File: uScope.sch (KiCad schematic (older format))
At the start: 20 parts

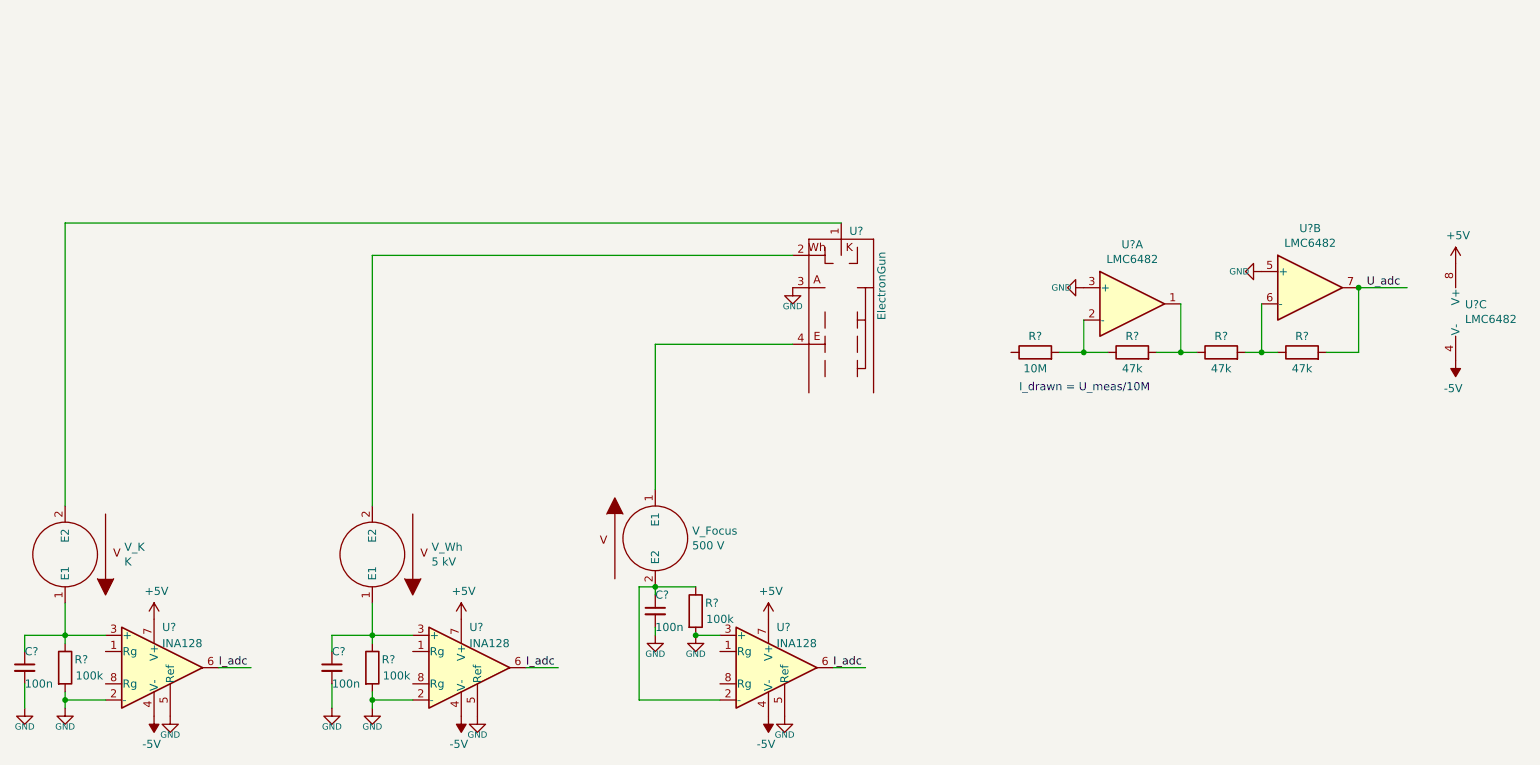
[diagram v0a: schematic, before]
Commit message: - schematic as hierarchical - added cache lib
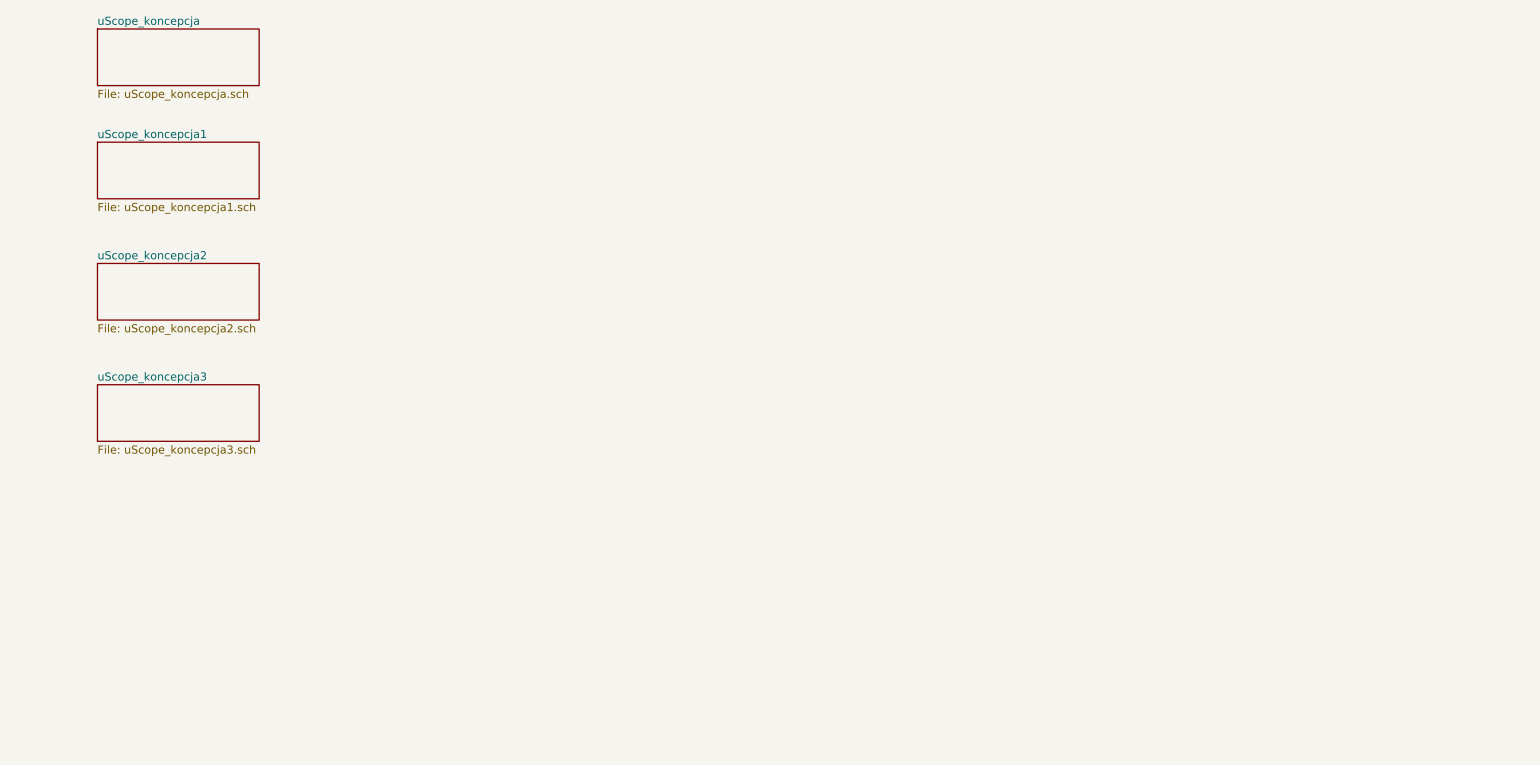
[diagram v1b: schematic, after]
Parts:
- removed C? (x3): 100n, symbol Device:C_Small
- removed R? (x3): 47k, symbol Device:R
- removed R?: 10M, symbol Device:R
- removed R? (x3): 100k, symbol Device:R
- removed U?: ElectronGun, symbol uScope:ElectronGun
- removed U? (x3): LMC6482, symbol Amplifier_Operational:LMC6482
- removed U? (x3): INA128, symbol Amplifier_Instrumentation:INA128
- removed V_Focus: 500 V, symbol pspice:VSOURCE
- removed V_K: K, symbol pspice:VSOURCE
- removed V_Wh: 5 kV, symbol pspice:VSOURCE
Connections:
- net labels removed: +5V, -5V, GND, I_adc, U_adc
- wire segments 46 -> 0
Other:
- note removed: "I_drawn = U_meas/10M"

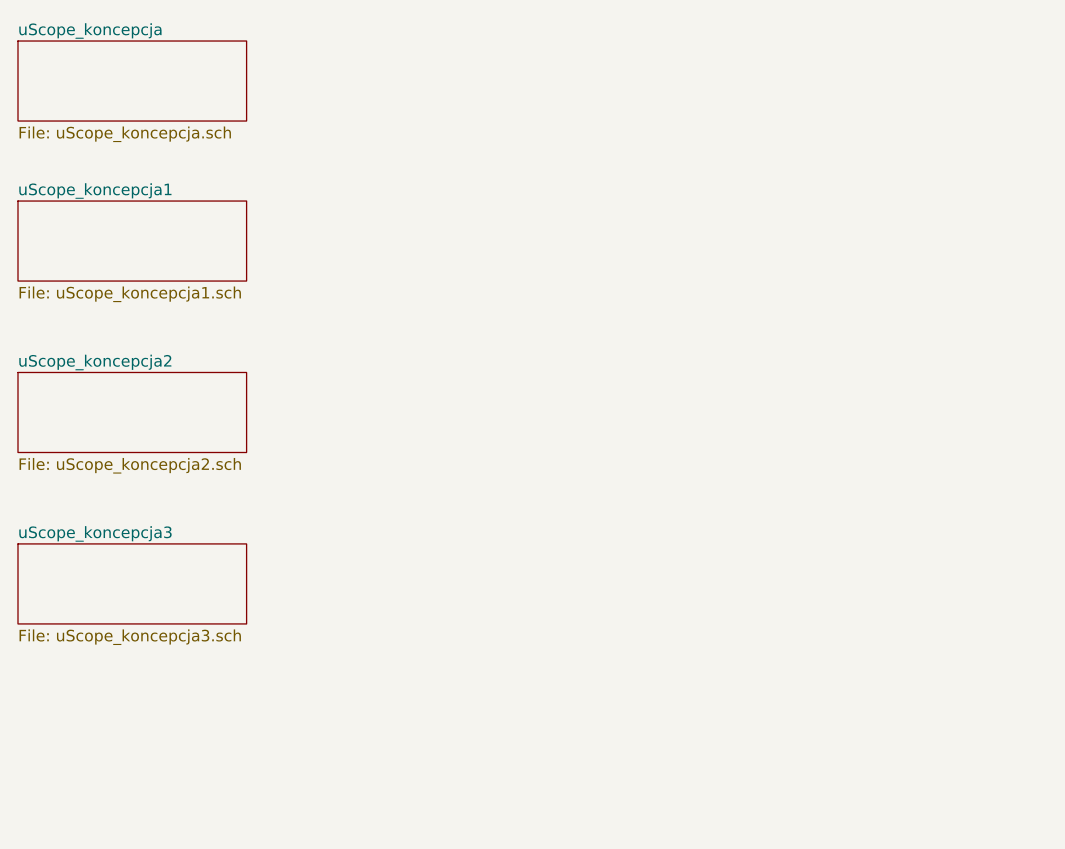
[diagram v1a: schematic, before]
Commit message: - moved voltmeters to separate sheet - hierarchical sheets
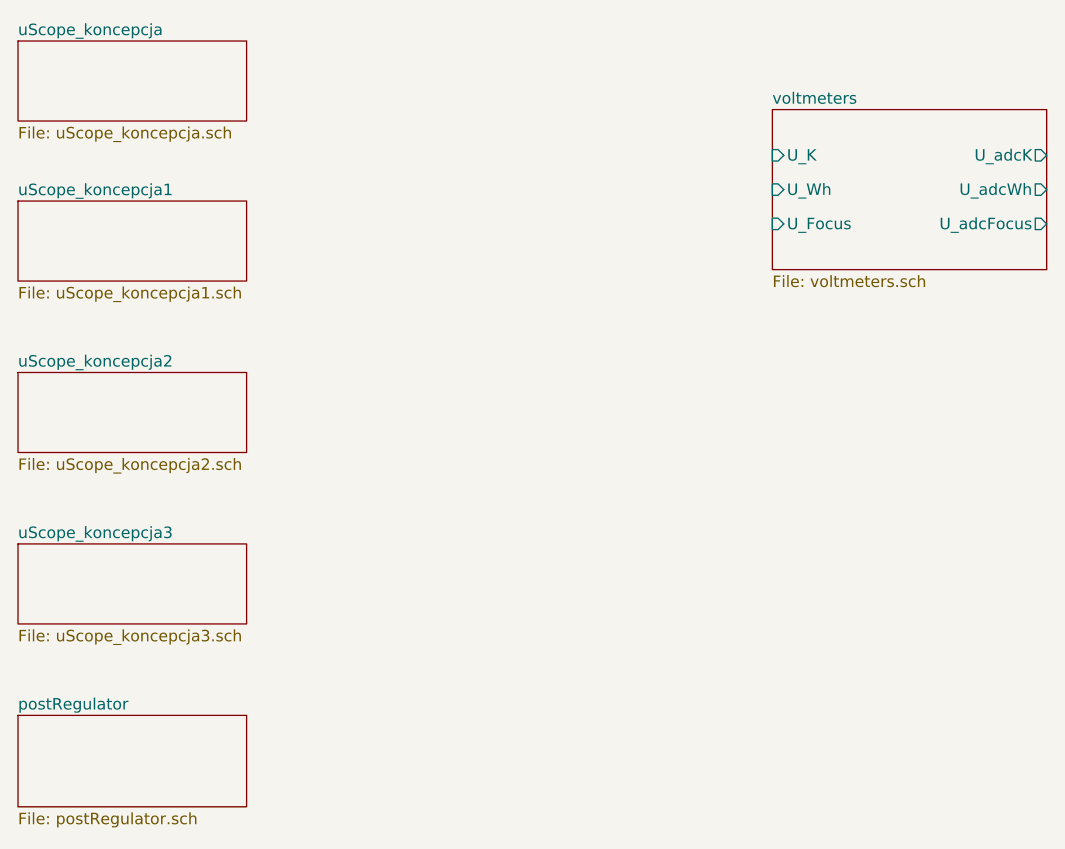
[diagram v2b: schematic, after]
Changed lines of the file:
@@
 $Descr A4 11693 8268
 encoding utf-8
-Sheet 1 5
+Sheet 1 7
 Title ""
 Date ""
@@
 F1 "uScope_koncepcja3.sch" 50
 $EndSheet
+$Sheet
+S 1350 3900 1000 400
+U 5F463F4C
+F0 "postRegulator" 50
+F1 "postRegulator.sch" 50
+$EndSheet
+$Sheet
+S 4650 1250 1200 700
+U 5F479892
+F0 "voltmeters" 50
+F1 "voltmeters.sch" 50
+F2 "U_Focus" I L 4650 1750 50
+F3 "U_K" I L 4650 1450 50
+F4 "U_Wh" I L 4650 1600 50
+F5 "U_adcFocus" O R 5850 1750 50
+F6 "U_adcK" O R 5850 1450 50
+F7 "U_adcWh" O R 5850 1600 50
+$EndSheet
 $EndSCHEMATC

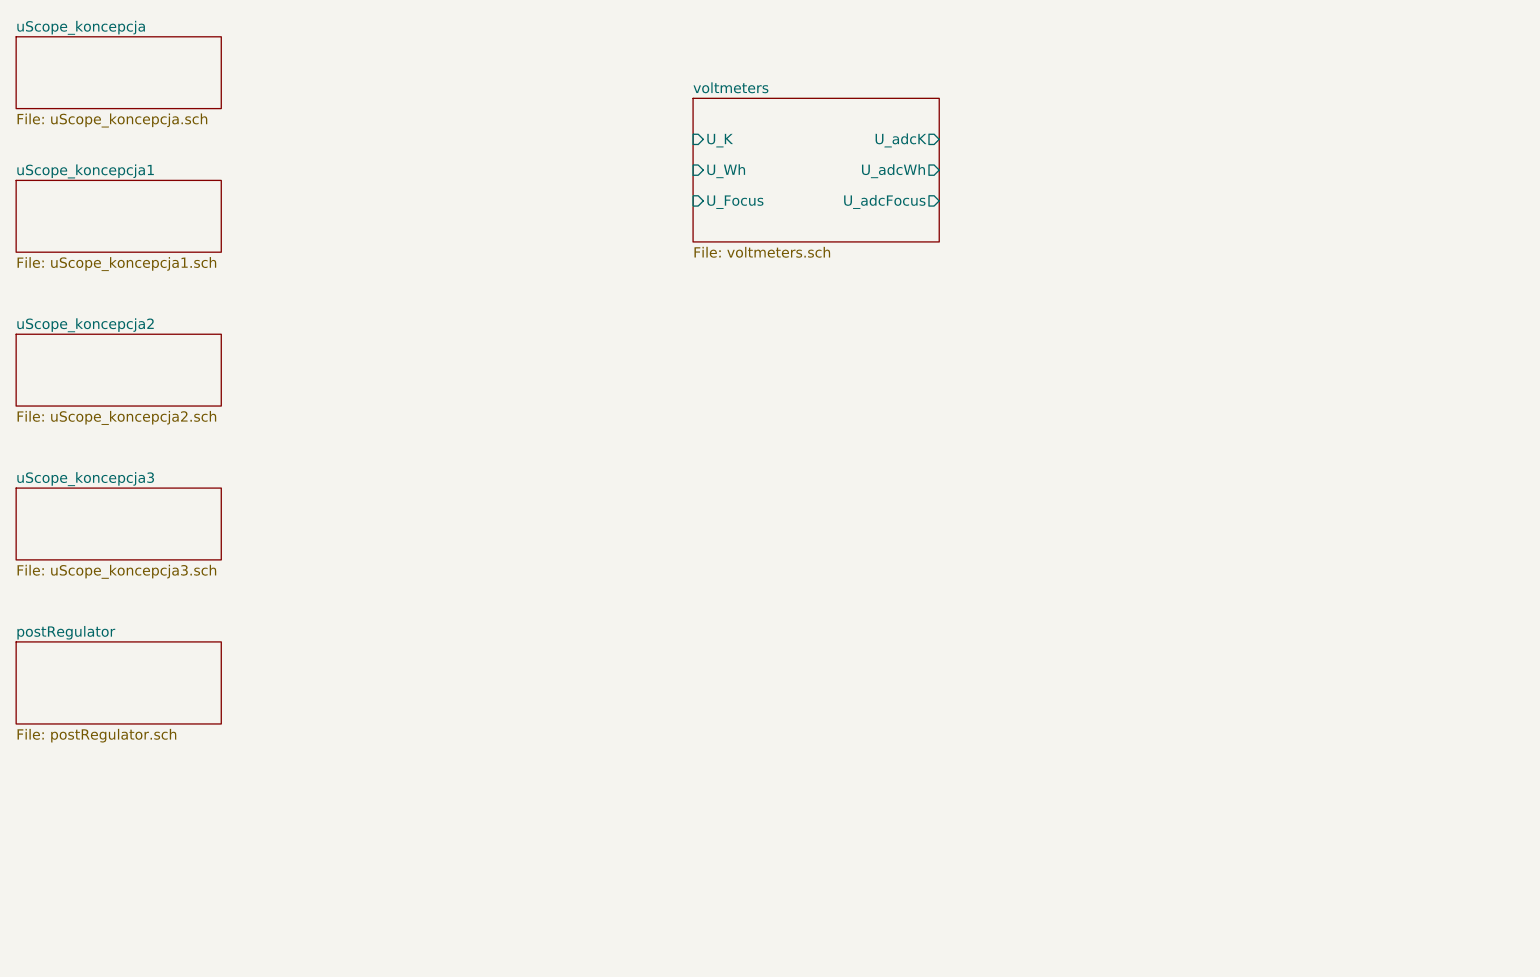
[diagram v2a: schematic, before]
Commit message: - added DC/DC converter to library, - moved ammeter & drivers to sub-sheet, - further develop
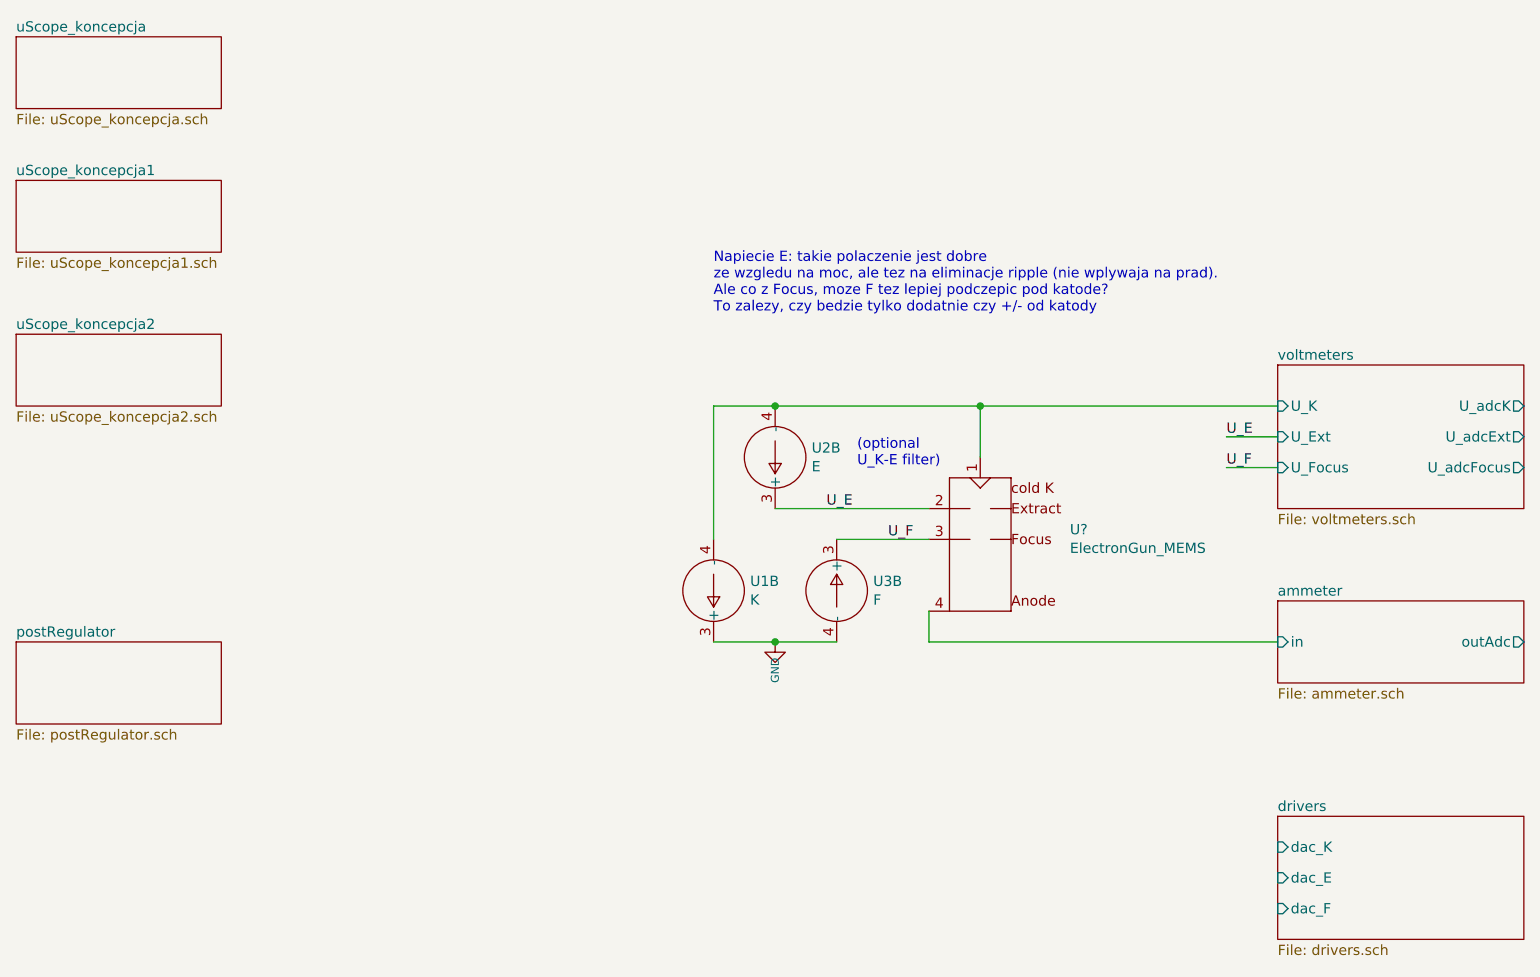
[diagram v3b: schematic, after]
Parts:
- added U1: K, symbol uScope:APD_P2_single
- added U2: E, symbol uScope:APD_P2_single
- added U3: F, symbol uScope:APD_P2_single
- added U?: ElectronGun_MEMS, symbol uScope:ElectronGun_MEMS
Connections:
- net voltmeters/U_K: now also U1.4 (-), U2.4 (-), U?.1 (Kathode)
- new net GND: U1.3 (+), U3.4 (-)
- new net U_E: U2.3 (+), U?.2 (Wehnelt)
- new net U_F: U3.3 (+), U?.3 (Anode)
- new net ammeter/in: U?.4 (Focus)
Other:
- note added: "(optional\nU_K-E filter)"
- note added: "Napiecie E: takie polaczenie jest dobre\nze wzgledu na moc, ale tez na eliminacje ripple (nie wplywaja na prad).\nAle co z Focus, moze F tez lepiej podczepic pod katode?\nTo zalezy, czy bedzie tylko dodatnie czy +/- od katody"
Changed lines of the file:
@@
 $Descr A4 11693 8268
 encoding utf-8
-Sheet 1 7
+Sheet 1 8
 Title ""
 Date ""
@@
 $EndSheet
 $Sheet
-S 1350 3150 1000 350
-U 5F40DCB9
-F0 "uScope_koncepcja3" 50
-F1 "uScope_koncepcja3.sch" 50
-$EndSheet
-$Sheet
 S 1350 3900 1000 400
 U 5F463F4C
@@
 $EndSheet
 $Sheet
-S 4650 1250 1200 700
+S 7500 2550 1200 700
 U 5F479892
 F0 "voltmeters" 50
 F1 "voltmeters.sch" 50
-F2 "U_Focus" I L 4650 1750 50
-F3 "U_K" I L 4650 1450 50
-F4 "U_Wh" I L 4650 1600 50
-F5 "U_adcFocus" O R 5850 1750 50
-F6 "U_adcK" O R 5850 1450 50
-F7 "U_adcWh" O R 5850 1600 50
+F2 "U_Focus" I L 7500 3050 50
+F3 "U_K" I L 7500 2750 50
+F4 "U_adcFocus" O R 8700 3050 50
+F5 "U_adcK" O R 8700 2750 50
+F6 "U_Ext" I L 7500 2900 50
+F7 "U_adcExt" O R 8700 2900 50
 $EndSheet
+Text Label 5600 3400 0    50   ~ 0
+U_F
+Wire Wire Line
+	6050 2750 6050 3000
+$Comp
+L uScope:ElectronGun_MEMS U?
+U 1 1 5F611500
+P 6050 3550
+F 0 "U?" H 6487 3748 50  0000 L CNN
+F 1 "ElectronGun_MEMS" H 6487 3657 50  0000 L CNN
+F 2 "" H 6050 3050 50  0001 C CNN
+F 3 "" H 6050 3050 50  0001 C CNN
+	1    6050 3550
+	1    0    0    -1
+$EndComp
+$Comp
+L uScope:APD_P2_single U1
+U 2 1 5F612D06
+P 4750 3650
+F 0 "U1" H 4572 3604 50  0000 R CNN
+F 1 "K" H 4572 3695 50  0000 R CNN
+F 2 "" H 4750 3650 50  0001 C CNN
+F 3 "" H 4750 3650 50  0001 C CNN
+	2    4750 3650
+	-1   0    0    1
+$EndComp
+$Comp
+L uScope:APD_P2_single U2
+U 2 1 5F612F4D
+P 5050 3000
+F 0 "U2" H 4872 2954 50  0000 R CNN
+F 1 "E" H 4872 3045 50  0000 R CNN
+F 2 "" H 5050 3000 50  0001 C CNN
+F 3 "" H 5050 3000 50  0001 C CNN
+	2    5050 3000
+	-1   0    0    1
+$EndComp
+$Comp
+L uScope:APD_P2_single U3
+U 2 1 5F612FE8
+P 5350 3650
+F 0 "U3" H 5528 3696 50  0000 L CNN
+F 1 "F" H 5528 3605 50  0000 L CNN
+F 2 "" H 5350 3650 50  0001 C CNN
+F 3 "" H 5350 3650 50  0001 C CNN
+	2    5350 3650
+	1    0    0    -1
+$EndComp
+Connection ~ 5050 2750
+Wire Wire Line
+	4750 2750 4750 3400
+Wire Wire Line
+	5350 3900 5050 3900
+Wire Wire Line
+	5800 3400 5350 3400
+Wire Wire Line
+	7500 2750 6050 2750
+Text Label 7250 3050 0    50   ~ 0
+U_F
+Text Label 5300 3250 0    50   ~ 0
+U_E
+Text Label 7250 2900 0    50   ~ 0
+U_E
+Wire Wire Line
+	7500 2900 7250 2900
+Wire Wire Line
+	7500 3050 7250 3050
+$Sheet
+S 7500 3700 1200 400
+U 5F618AB9
+F0 "ammeter" 50
+F1 "ammeter.sch" 50
+F2 "in" I L 7500 3900 50
+F3 "outAdc" O R 8700 3900 50
+$EndSheet
+Wire Wire Line
+	7500 3900 5800 3900
+$Comp
+L power:GND #PWR?
+U 1 1 5F61B422
+P 5050 3900
+AR Path="/5F40DCB9/5F61B422" Ref="#PWR?"  Part="1"
+AR Path="/5F618AB9/5F61B422" Ref="#PWR?"  Part="1"
+AR Path="/5F61B422" Ref="#PWR?"  Part="1"
+F 0 "#PWR?" H 5050 3740 50  0001 C CNN
+F 1 "GND" V 5050 3823 39  0000 R CNN
+F 2 "" H 5050 3900 50  0001 C CNN
+F 3 "" H 5050 3900 50  0001 C CNN
+	1    5050 3900
+	1    0    0    -1
+$EndComp
+Connection ~ 5050 3900
+Wire Wire Line
+	5050 3900 4750 3900
+$Sheet
+S 7500 4750 1200 600
+U 5F61C123
+F0 "drivers" 50
+F1 "drivers.sch" 50
+F2 "dac_K" I L 7500 4900 50
+F3 "dac_F" I L 7500 5200 50
+F4 "dac_E" I L 7500 5050 50
+$EndSheet
+Text Notes 4750 2300 0    50   ~ 0
+Napiecie E: takie polaczenie jest dobre\nze wzgledu na moc, ale tez na eliminacje ripple (nie wplywaja na prad).\nAle co z Focus, moze F tez lepiej podczepic pod katode?\nTo zalezy, czy bedzie tylko dodatnie czy +/- od katody
+Wire Wire Line
+	4750 2750 5050 2750
+Wire Wire Line
+	5050 3250 5800 3250
+Wire Wire Line
+	5050 2750 6050 2750
+Connection ~ 6050 2750
+Text Notes 5450 3050 0    50   ~ 0
+(optional\nU_K-E filter)
+Wire Wire Line
+	5800 3900 5800 3750
 $EndSCHEMATC
